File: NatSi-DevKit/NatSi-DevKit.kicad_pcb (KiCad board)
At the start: 4 copper layers, 0 parts

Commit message: some updates schematic
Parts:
- added J1: USB_C_Receptacle_USB2.0_16P, sumec_brd:USB_Type_C, F.Cu at (43.2, 16.9)
- added U1: ESP32-S3-WROOM-1, PCM_Espressif:ESP32-S3-WROOM-1, F.Cu at (9.86, 16.1)
- added U2: NCP1117-3.3_SOT223, Package_TO_SOT_SMD:SOT-223-3_TabPin2, F.Cu at (25.1, 13.8)

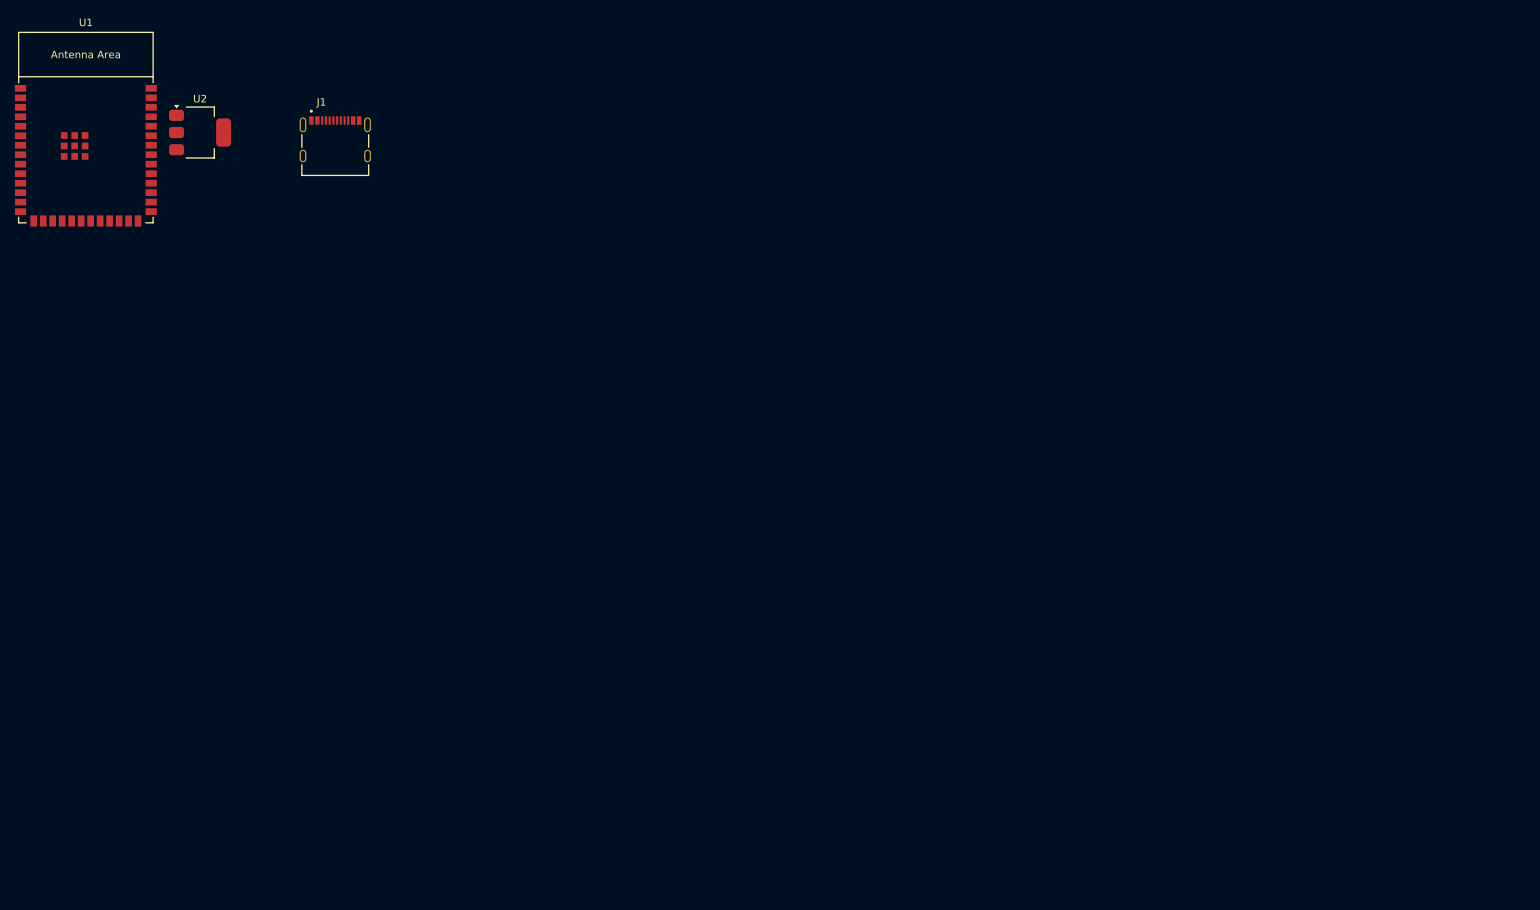
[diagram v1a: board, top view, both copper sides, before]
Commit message: Schematic update
Blocks, schematic finished
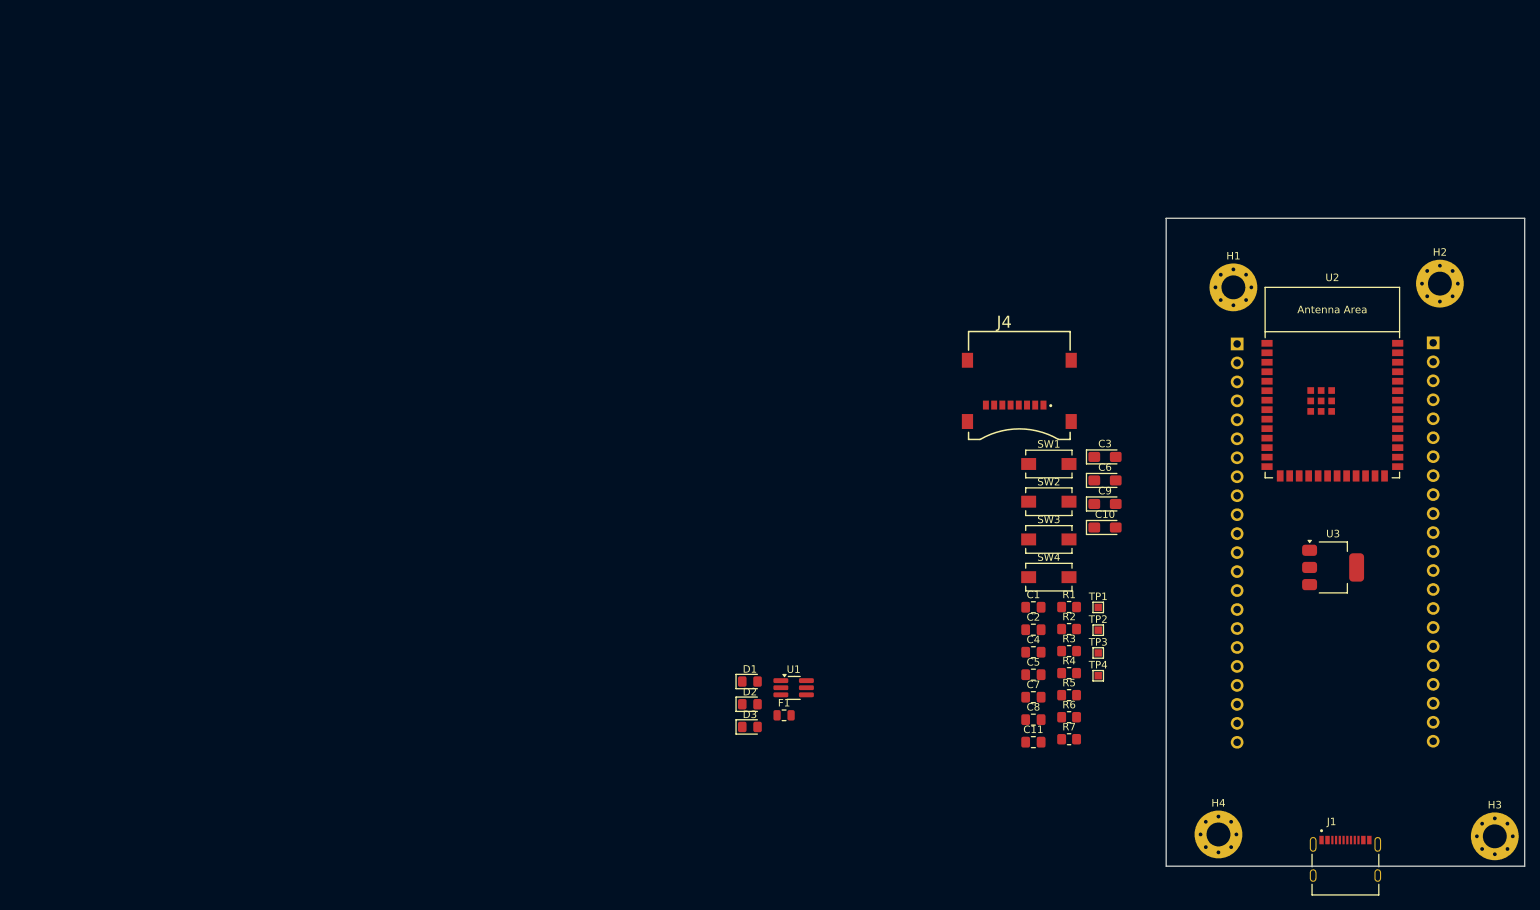
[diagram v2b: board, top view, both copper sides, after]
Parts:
- added C1: 100nF, Capacitor_SMD:C_0805_2012Metric_Pad1.18x1.45mm_HandSolder, F.Cu at (136.7, 77.3)
- added C10: 10uF, Capacitor_Tantalum_SMD:CP_EIA-3216-18_Kemet-A_Pad1.58x1.35mm_HandSolder, F.Cu at (146.3, 66.7)
- added C11: 100nF, Capacitor_SMD:C_0805_2012Metric_Pad1.18x1.45mm_HandSolder, F.Cu at (136.7, 95.4)
- added C2: 100nF, Capacitor_SMD:C_0805_2012Metric_Pad1.18x1.45mm_HandSolder, F.Cu at (136.7, 80.3)
- added C3: 10uF, Capacitor_Tantalum_SMD:CP_EIA-3216-18_Kemet-A_Pad1.58x1.35mm_HandSolder, F.Cu at (146.3, 57.2)
- added C4: 100nF, Capacitor_SMD:C_0805_2012Metric_Pad1.18x1.45mm_HandSolder, F.Cu at (136.7, 83.3)
- added C5: 100nF, Capacitor_SMD:C_0805_2012Metric_Pad1.18x1.45mm_HandSolder, F.Cu at (136.7, 86.4)
- added C6: 10uF, Capacitor_Tantalum_SMD:CP_EIA-3216-18_Kemet-A_Pad1.58x1.35mm_HandSolder, F.Cu at (146.3, 60.4)
- added C7: 100nF, Capacitor_SMD:C_0805_2012Metric_Pad1.18x1.45mm_HandSolder, F.Cu at (136.7, 89.4)
- added C8: 100nF, Capacitor_SMD:C_0805_2012Metric_Pad1.18x1.45mm_HandSolder, F.Cu at (136.7, 92.4)
- added C9: 10uF, Capacitor_Tantalum_SMD:CP_EIA-3216-18_Kemet-A_Pad1.58x1.35mm_HandSolder, F.Cu at (146.3, 63.5)
- added D1: LED, LED_SMD:LED_0805_2012Metric_Pad1.15x1.40mm_HandSolder, F.Cu at (98.8, 87.3)
- added D2: LED, LED_SMD:LED_0805_2012Metric_Pad1.15x1.40mm_HandSolder, F.Cu at (98.8, 90.3)
- added D3: LED, LED_SMD:LED_0805_2012Metric_Pad1.15x1.40mm_HandSolder, F.Cu at (98.8, 93.4)
- added F1: Polyfuse, Fuse:Fuse_0805_2012Metric, F.Cu at (103.3, 91.8)
- added H1: Mounting Hole M3, MountingHole:MountingHole_3.2mm_M3_Pad_Via, F.Cu at (163.5, 34.5)
- added H2: Mounting Hole M3, MountingHole:MountingHole_3.2mm_M3_Pad_Via, F.Cu at (191.2, 34.0)
- added H3: Mounting Hole M3, MountingHole:MountingHole_3.2mm_M3_Pad_Via, F.Cu at (198.5, 108.0)
- added H4: Mounting Hole M3, MountingHole:MountingHole_3.2mm_M3_Pad_Via, F.Cu at (161.5, 107.8)
- added J2: Conn_01x22_Pin, Connector_PinHeader_2.54mm:PinHeader_1x22_P2.54mm_Vertical, B.Cu at (164.0, 42.1)
- added J3: Conn_01x22_Pin, Connector_PinHeader_2.54mm:PinHeader_1x22_P2.54mm_Vertical, B.Cu at (190.2, 41.9)
- added J4: MEM2067-02-180-00-A_REVB, Schrack_brd:MICRO_SD_CARD, F.Cu at (134.8, 47.6)
- added R1: 10k, Resistor_SMD:R_0805_2012Metric_Pad1.20x1.40mm_HandSolder, F.Cu at (141.5, 77.3)
- added R2: 15R, Resistor_SMD:R_0805_2012Metric_Pad1.20x1.40mm_HandSolder, F.Cu at (141.5, 80.2)
- added R3: 15R, Resistor_SMD:R_0805_2012Metric_Pad1.20x1.40mm_HandSolder, F.Cu at (141.5, 83.2)
- added R4: 10k, Resistor_SMD:R_0805_2012Metric_Pad1.20x1.40mm_HandSolder, F.Cu at (141.5, 86.2)
- added R5: 100R, Resistor_SMD:R_0805_2012Metric_Pad1.20x1.40mm_HandSolder, F.Cu at (141.5, 89.1)
- added R6: 100R, Resistor_SMD:R_0805_2012Metric_Pad1.20x1.40mm_HandSolder, F.Cu at (141.5, 92.0)
- added R7: 100R, Resistor_SMD:R_0805_2012Metric_Pad1.20x1.40mm_HandSolder, F.Cu at (141.5, 95.0)
- added SW1: SW_Push, Button_Switch_SMD:SW_SPST_EVQPE1, F.Cu at (138.8, 58.1)
- added SW2: SW_Push, Button_Switch_SMD:SW_SPST_EVQPE1, F.Cu at (138.8, 63.2)
- added SW3: SW_Push, Button_Switch_SMD:SW_SPST_EVQPE1, F.Cu at (138.8, 68.2)
- added SW4: SW_Push, Button_Switch_SMD:SW_SPST_EVQPE1, F.Cu at (138.8, 73.3)
- added TP1: TestPoint, TestPoint:TestPoint_Pad_1.0x1.0mm, F.Cu at (145.4, 77.3)
- added TP2: TestPoint, TestPoint:TestPoint_Pad_1.0x1.0mm, F.Cu at (145.4, 80.4)
- added TP3: TestPoint, TestPoint:TestPoint_Pad_1.0x1.0mm, F.Cu at (145.4, 83.5)
- added TP4: TestPoint, TestPoint:TestPoint_Pad_1.0x1.0mm, F.Cu at (145.4, 86.5)
- added U3: NCP1117-3.3_SOT223, Package_TO_SOT_SMD:SOT-223-3_TabPin2, F.Cu at (176.8, 72.0)
- J1: value USB_C_Receptacle_USB2.0_16P -> USB_TypeC
- U1: value ESP32-S3-WROOM-1 -> USBLC6-2SC6; footprint PCM_Espressif:ESP32-S3-WROOM-1 -> Package_TO_SOT_SMD:TSOT-23-6_HandSoldering
- U2: value NCP1117-3.3_SOT223 -> ESP32-S3-WROOM-1; footprint Package_TO_SOT_SMD:SOT-223-3_TabPin2 -> PCM_Espressif:ESP32-S3-WROOM-1
- moved J1 166.1 mm to (178.5, 113.2)
- moved U2 155.9 mm to (176.8, 50.2)
- moved U1 119.0 mm to (104.6, 88.1)
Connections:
- J1 pad A1_B12: (no net) -> GND
- J1 pad A4_B9: (no net) -> Net-(F1-Pad2)
- J1 pad A6: unconnected-(J1-D+-PadA6) -> D+ IN
- J1 pad A7: unconnected-(J1-D--PadA7) -> D- IN
- J1 pad B1_A12: (no net) -> GND
- J1 pad B4_A9: (no net) -> Net-(F1-Pad2)
- J1 pad B6: unconnected-(J1-D+-PadB6) -> D+ IN
- J1 pad B7: unconnected-(J1-D--PadB7) -> D- IN
- J1 pad S1: unconnected-(J1-SHIELD-PadS1) -> GND
- J1 pad S2: (no net) -> GND
- J1 pad S3: (no net) -> GND
- J1 pad S4: (no net) -> GND
- U1 pad 1: Net-(U1-GND-Pad1) -> Net-(R2-Pad2)
- U1 pad 2: +3V3 -> GND
- U1 pad 3: unconnected-(U1-EN-Pad3) -> Net-(R3-Pad2)
- U1 pad 4: unconnected-(U1-IO4-Pad4) -> D-
- U1 pad 5: unconnected-(U1-IO5-Pad5) -> VBUS 5V
- U1 pad 6: unconnected-(U1-IO6-Pad6) -> D+
- U2 pad 1: unconnected-(U2-GND-Pad1) -> GND
- U2 pad 2: unconnected-(U2-VO-Pad2) -> +3V3
- U2 pad 3: +5V -> EN
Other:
- board outline added: 48 x 86.8 mm

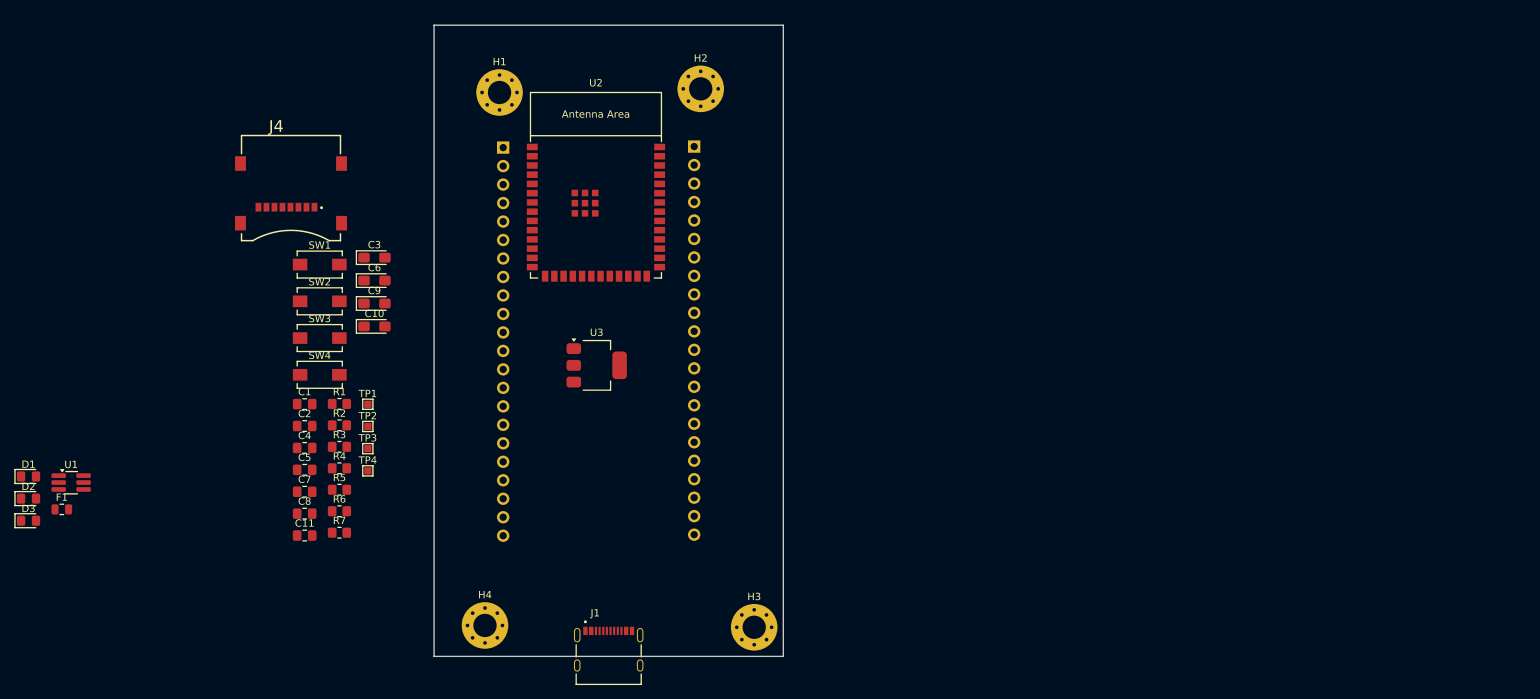
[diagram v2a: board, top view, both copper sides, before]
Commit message: PCB Layut update
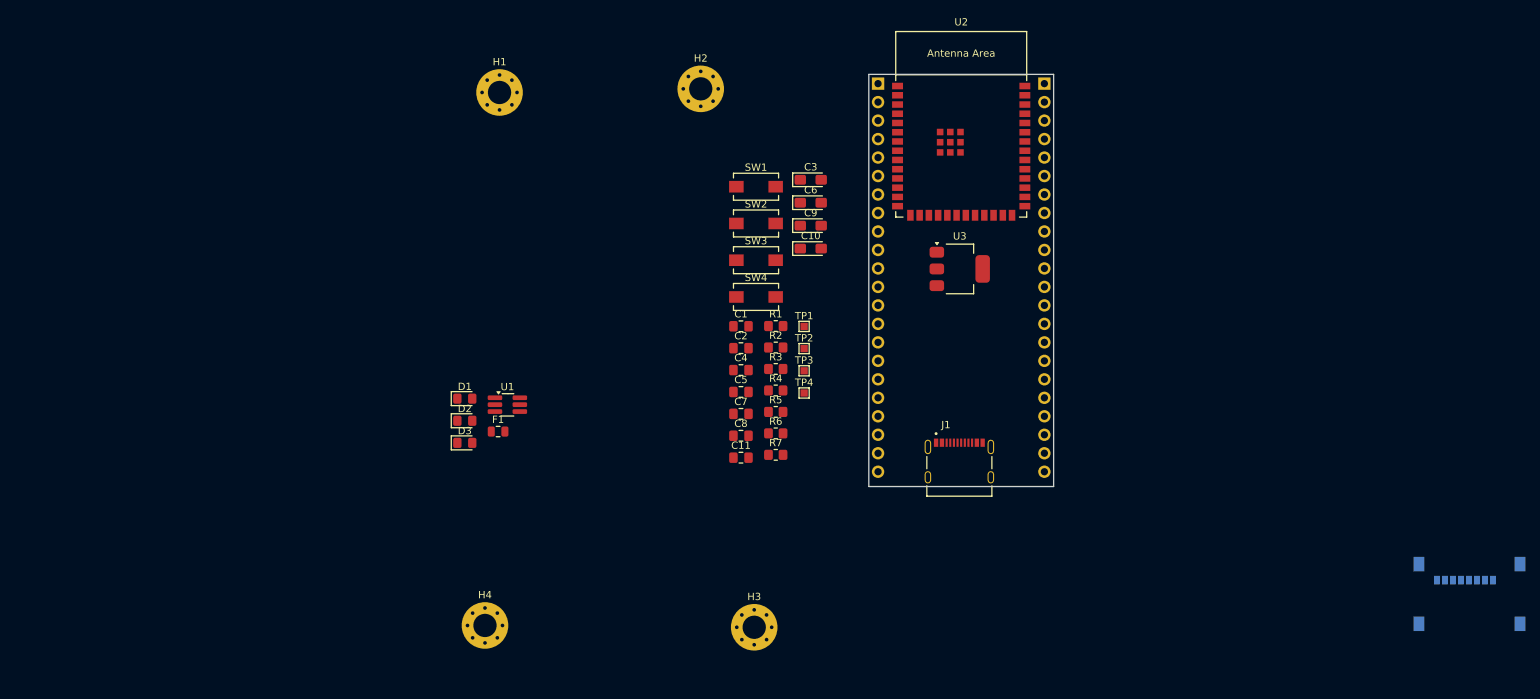
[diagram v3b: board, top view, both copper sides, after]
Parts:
- J4: moved to B.Cu
- moved J4 171.5 mm to (296.8, 104.1)
- moved C1 60.9 mm to (196.7, 66.6)
- moved C10 60.9 mm to (206.3, 56.0)
- moved C11 60.9 mm to (196.7, 84.7)
- moved C2 60.9 mm to (196.7, 69.6)
- moved C3 60.9 mm to (206.3, 46.5)
- moved C4 60.9 mm to (196.7, 72.7)
- moved C5 60.9 mm to (196.7, 75.7)
- moved C6 60.9 mm to (206.3, 49.6)
- moved C7 60.9 mm to (196.7, 78.7)
- moved C8 60.9 mm to (196.7, 81.7)
- moved C9 60.9 mm to (206.3, 52.8)
- moved F1 60.9 mm to (163.3, 81.1)
- moved R1 60.9 mm to (201.5, 66.6)
- moved R2 60.9 mm to (201.5, 69.5)
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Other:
- board size 48 x 86.8 mm -> 25.4 x 56.6 mm

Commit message: layout update
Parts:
- removed the F1 at (163.3, 81.1)
- removed the R1 at (201.5, 66.6)
- added C12: 100nF, Capacitor_SMD:C_0805_2012Metric_Pad1.18x1.45mm_HandSolder, F.Cu at (232.1, 53.8)
- added C21: 100nF, Capacitor_SMD:C_0805_2012Metric_Pad1.18x1.45mm_HandSolder, F.Cu at (251.7, 77.5)
- added D4: LED, LED_SMD:LED_0805_2012Metric_Pad1.15x1.40mm_HandSolder, F.Cu at (208.6, 58.2)
- added F1: Polyfuse, Fuse:Fuse_0805_2012Metric, F.Cu at (227.8, 84.6)
- added F1: Polyfuse/50R, Fuse:Fuse_0805_2012Metric, B.Cu at (249.7, 77.8)
- added J2: USB_TypeC, sumec_brd:USB_Type_C, F.Cu at (248.6, 85.5)
- added R1: 10k, Resistor_SMD:R_0805_2012Metric_Pad1.20x1.40mm_HandSolder, F.Cu at (249.7, 77.5)
- added R1: 100k, Resistor_SMD:R_0805_2012Metric_Pad1.20x1.40mm_HandSolder, F.Cu at (222.0, 84.4)
- added R12: 15R, Resistor_SMD:R_0805_2012Metric_Pad1.20x1.40mm_HandSolder, F.Cu at (247.8, 77.5)
- added R13: 15R, Resistor_SMD:R_0805_2012Metric_Pad1.20x1.40mm_HandSolder, F.Cu at (245.8, 77.5)
- added R8: 100R, Resistor_SMD:R_0805_2012Metric_Pad1.20x1.40mm_HandSolder, F.Cu at (208.6, 62.3)
- added U3: USBLC6-2SC6, Package_TO_SOT_SMD:TSOT-23-6_HandSoldering, B.Cu at (277.8, 83.0)
- C11, C4, C7: value 100nF -> 10uF; footprint Capacitor_SMD:C_0805_2012Metric_Pad1.18x1.45mm_HandSolder -> Capacitor_Tantalum_SMD:CP_EIA-3216-18_Kemet-A_Pad1.58x1.35mm_HandSolder
- C3, C6, C9: value 10uF -> 100nF; footprint Capacitor_Tantalum_SMD:CP_EIA-3216-18_Kemet-A_Pad1.58x1.35mm_HandSolder -> Capacitor_SMD:C_0805_2012Metric_Pad1.18x1.45mm_HandSolder
- D1: value LED -> D_Schottky; footprint LED_SMD:LED_0805_2012Metric_Pad1.15x1.40mm_HandSolder -> Diode_SMD:D_1206_3216Metric_Pad1.42x1.75mm_HandSolder
- H1, H2, H3, H4: footprint MountingHole:MountingHole_3.2mm_M3_Pad_Via -> MountingHole:MountingHole_2.1mm
- R2: value 15R -> 10k
- R4: value 10k -> 15R
- R5: value 100R -> 10k
- moved J4 95.3 mm to (226.9, 39.4)
- moved D1 71.6 mm to (229.9, 83.8), turned to -90 degrees
- moved U1 62.3 mm to (226.8, 79.5), turned to 90 degrees
- moved H3 59.2 mm to (155.6, 67.2)
- moved D3 52.8 mm to (205.6, 58.2), turned to 90 degrees
- moved SW2 52.0 mm to (234.3, 90.4), turned to 90 degrees
- moved D2 48.7 mm to (202.5, 58.2), turned to 90 degrees
- moved SW1 47.8 mm to (219.6, 90.4), turned to 90 degrees
- moved H2 44.9 mm to (155.6, 61.5)
- moved C11 44.0 mm to (231.5, 57.8), turned to 180 degrees
- moved C3 42.7 mm to (232.1, 80.6), turned to 90 degrees
- moved C1 39.6 mm to (232.1, 84.4), turned to -90 degrees
- moved R5 38.1 mm to (232.1, 55.7)
- moved C6 38.1 mm to (229.9, 79.5), turned to 90 degrees
- moved H4 35.3 mm to (155.6, 73.0)
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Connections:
- C1 pad 1: EN -> GND
- C1 pad 2: GND -> /SHLD
- C2 pad 1: BOOT -> EN
- C3 pad 1: +3V3 -> BOOT
- C5 pad 1: VBUS 5V -> +3V3
- C7 pad 1: GND -> +5V
- C7 pad 2: +5V -> GND
- C8 pad 2: +3.3V -> +5V
- C9 pad 1: +3.3V -> GND
- C9 pad 2: GND -> +3V3
- D1 pad 1: Net-(D1-K) -> +5V
- D1 pad 2: +3.3V -> Net-(D1-A)
- D2 pad 2: LED1 -> +3.3V
- D3 pad 2: LED2 -> LED1
- J1 pad S1: GND -> /SHLD
- J1 pad S2: GND -> /SHLD
- J1 pad S3: GND -> /SHLD
- J1 pad S4: GND -> /SHLD
- R2 pad 1: D+ IN -> EN
- R2 pad 2: Net-(R2-Pad2) -> +3V3
- R3 pad 1: D- IN -> D+ IN
- R4 pad 1: IO10_~{CS} -> D- IN
- R4 pad 2: +3V3 -> Net-(R4-Pad2)
- R5 pad 1: Net-(D1-K) -> IO10_~{CS}
- R5 pad 2: GND -> +3V3
- U1 pad 1: Net-(R2-Pad2) -> Net-(R3-Pad2)
- U1 pad 3: Net-(R3-Pad2) -> Net-(R4-Pad2)
- U1 pad 5: VBUS 5V -> +5V
- U3 pad 2: +3.3V -> +3V3
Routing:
- net (no net): track 0.00 -> 12.5 mm, vias 0 -> 3
- net GND: track 0.00 -> 10.4 mm
- net D- IN: track 0.00 -> 9.96 mm
- net VBUS 5V: track 0.00 -> 7.54 mm, vias 0 -> 1
- net D+ IN: track 0.00 -> 7.36 mm
- net Net-(F1-Pad2): track 0.00 -> 7.35 mm
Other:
- board size 25.4 x 56.6 mm -> 25.4 x 62.7 mm

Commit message: pcb layout
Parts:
- removed C21: 100nF, Capacitor_SMD:C_0805_2012Metric_Pad1.18x1.45mm_HandSolder
- removed the F1 at (249.7, 77.8)
- removed H1, H2, H3, H4: Mounting Hole M3, MountingHole:MountingHole_2.1mm
- removed the J2 at (248.6, 85.5)
- removed the R1 at (249.7, 77.5)
- removed R12, R13: 15R, Resistor_SMD:R_0805_2012Metric_Pad1.20x1.40mm_HandSolder
- removed the R7 at (205.6, 62.3)
- removed SW4: SW_Push, Button_Switch_SMD:SW_SPST_EVQPE1
- removed the U3 at (277.8, 83.0)
- added C6: 100nF, Capacitor_SMD:C_0805_2012Metric_Pad1.18x1.45mm_HandSolder, F.Cu at (222.2, 65.6)
- added R10: 100R, Resistor_SMD:R_0805_2012Metric_Pad1.20x1.40mm_HandSolder, F.Cu at (232.9, 61.8)
- added R5: 1k, Resistor_SMD:R_0805_2012Metric_Pad1.20x1.40mm_HandSolder, F.Cu at (222.2, 61.8)
- added R9: 100R, Resistor_SMD:R_0805_2012Metric_Pad1.20x1.40mm_HandSolder, F.Cu at (231.0, 61.8)
- R6: value 100R -> 10k
- TP1, TP2, TP3: footprint TestPoint:TestPoint_Pad_1.0x1.0mm -> TestPoint:TestPoint_THTPad_D1.5mm_Drill0.7mm
- TP4: footprint TestPoint:TestPoint_Pad_1.0x1.0mm -> sumec_graphic:NATI_PICME_IMG
- moved TP4 36.1 mm to (228.9, 55.9)
- moved SW3 32.0 mm to (219.1, 63.8), turned to 90 degrees
- moved D2 27.5 mm to (229.0, 65.5)
- moved D3 26.4 mm to (231.0, 65.5)
- moved D4 25.4 mm to (232.9, 65.5)
- moved R6 21.6 mm to (224.1, 61.8), turned to 90 degrees
- moved R8 20.4 mm to (229.0, 61.8)
- moved TP3 18.8 mm to (219.6, 75.4)
- moved C7 5.10 mm to (225.0, 80.7), turned to -90 degrees
- moved C12 4.24 mm to (235.0, 55.4), turned to -90 degrees
- moved C2 3.96 mm to (221.1, 84.5), turned to -90 degrees
- moved C3 3.91 mm to (232.7, 84.4)
- moved D1 3.84 mm to (230.8, 80.1)
- moved C4 3.11 mm to (218.8, 55.4), turned to -90 degrees
- moved TP2 1.87 mm to (219.6, 72.8)
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- renumbered C9 to C10, C10 to C11, C11 to C12, C12 to C13, C6 to C7, C7 to C8, C8 to C9, R5 to R7
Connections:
- D2 pad 1: Net-(D2-K) -> GND
- D2 pad 2: +3.3V -> Net-(D2-A)
- D3 pad 1: Net-(D3-K) -> GND
- D3 pad 2: LED1 -> Net-(D3-A)
- D4 pad 1: Net-(D4-K) -> GND
- D4 pad 2: LED2 -> Net-(D4-A)
- R6 pad 1: Net-(D2-K) -> BT1
- R6 pad 2: GND -> +3V3
- R8 pad 1: Net-(D4-K) -> +3V3
- R8 pad 2: GND -> Net-(D2-A)
- SW3 pad 1: +3V3 -> GND
- SW3 pad 2: TEST PROGRAM 1 -> Net-(R5-Pad1)
- TP3 pad 1: unconnected-(TP3-Pad1) -> GND
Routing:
- net +5V: track 0.00 -> 19.7 mm
- net (no net): track 12.5 -> 0.00 mm, vias 3 -> 0
- net GND: track 10.4 -> 0.00 mm
- net +3V3: track 0.00 -> 8.92 mm
- net VBUS 5V: track 7.54 -> 0.00 mm, vias 1 -> 0
- net /SHLD: track 0.00 -> 6.44 mm
- net Net-(R4-Pad2): track 0.00 -> 4.58 mm, vias 0 -> 2
- net D- IN: track 9.96 -> 5.96 mm
- net Net-(F1-Pad2): track 7.35 -> 10.3 mm
- net Net-(D1-A): track 0.00 -> 2.81 mm
- net D+ IN: track 7.36 -> 4.60 mm
- net Net-(R3-Pad2): track 0.00 -> 2.16 mm
- added copper zone on B.Cu, net /SHLD
- added copper zone on B.Cu, net GND
- added copper zone on F.Cu, net GND
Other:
- board size 25.4 x 62.7 mm -> 25.4 x 62.5 mm
